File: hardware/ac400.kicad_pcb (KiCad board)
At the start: 2 copper layers, 105.4 x 76.2 mm, 71 parts, among them J1 AVR-ISP-10, J2 LOW OUT, J3 MID OUT, J4 HIGH OUT, J5 COMMON OUT, J6 COMMON IN, J7 LINE IN, J8 3.3V IN, K1 SRD-03VDC-SL-C, K2 SRD-03VDC-SL-C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

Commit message: "final" touches on v1 board
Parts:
- added SYM2: Julian7 logo, ac400:Julian7 maker's mark, F.Cu at (148.1, 117.3)
- C2: footprint PCM_Capacitor_THT_AKL:C_Radial_D8.0mm_H11.5mm_P3.50mm -> Capacitor_THT:CP_Radial_D8.0mm_P3.50mm
- D1, D2, D3: footprint Diode_SMD:D_0805_2012Metric_Pad1.15x1.40mm_HandSolder -> Diode_SMD:D_SOD-323
- TP5: value MG -> MD
- TP6: value MD -> MG
- TP7: value HG -> HD
- TP8: value HD -> HG
- moved R16 8.70 mm to (171.2, 116.5), turned to 90 degrees
- moved C13 5.39 mm to (85.1, 120.5), turned to 90 degrees
- moved R17 5.16 mm to (86.9, 126.1), turned to 90 degrees
- moved C2 3.98 mm to (115.3, 97.9), turned to 90 degrees
- moved TP8 3.56 mm to (137.2, 89.0)
- moved JP1 3.16 mm to (173.7, 108.6), turned to 90 degrees
- moved TP6 3.11 mm to (154.7, 89.0), turned to 180 degrees
- moved TP5 2.96 mm to (154.7, 92.0), turned to 180 degrees
- moved R1 2.74 mm to (170.3, 96.2)
- moved Q4 2.45 mm to (90.4, 126.1), turned to -90 degrees
- moved TP7 2.44 mm to (137.2, 92.0)
- moved C8 1.88 mm to (131.1, 94.2), turned to 90 degrees
- moved C6 1.86 mm to (165.6, 94.2), turned to 90 degrees
- moved C9 1.85 mm to (163.2, 94.2), turned to 90 degrees
- moved TP3 1.82 mm to (173.0, 92.0)
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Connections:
- net Net-(BZ1--) renamed /Buzz Drain
- net Net-(D1-A) renamed /Low Drain
- net Net-(J2-Pin_1) renamed /LOW OUT
- net Net-(J3-Pin_1) renamed /MID OUT
- net Net-(J4-Pin_1) renamed /HIGH OUT
- D2 pad 2: Net-(D2-A) -> /Mid Drain
- D3 pad 2: Net-(D3-A) -> /High Drain
- K2 pad 2: Net-(D2-A) -> /Mid Drain
- K3 pad 2: Net-(D3-A) -> /High Drain
- Q2 pad 3: Net-(D2-A) -> /Mid Drain
- Q3 pad 3: Net-(D3-A) -> /High Drain
- TP5 pad 1: Net-(Q2-G) -> /Mid Drain
- TP6 pad 1: Net-(D2-A) -> Net-(Q2-G)
- TP7 pad 1: Net-(Q3-G) -> /High Drain
- TP8 pad 1: Net-(D3-A) -> Net-(Q3-G)
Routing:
- net +3.3V: track 274.7 -> 250.3 mm
- net Net-(D2-A): track 21.8 -> 0.00 mm, vias 2 -> 0
- net Net-(D3-A): track 21.6 -> 0.00 mm, vias 2 -> 0
- net /Mid Drain: track 0.00 -> 21.0 mm, vias 0 -> 2
- net /High Drain: track 0.00 -> 20.8 mm, vias 0 -> 2
- net Net-(Q3-G): track 19.8 -> 10.7 mm
- net BUZZ: track 71.4 -> 77.5 mm
- net HIGH: track 35.2 -> 40.8 mm
- net Net-(Q2-G): track 14.8 -> 10.2 mm
- net Net-(Q4-G): track 8.82 -> 4.87 mm
- net NEUT: track 39.8 -> 43.7 mm
- net MISO: track 20.3 -> 16.9 mm
- net LOW: track 15.9 -> 13.2 mm
- net Net-(Q1-G): track 12.7 -> 10.7 mm
- net GND: track 26.8 -> 25.2 mm, vias 101 -> 107
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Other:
- board text added: "AC-400 controller"
- board text added: "COMMON IN"
- board text added: "COMMON OUT"
- board text added: "HIGH OUT"
- board text added: "LINE IN"
- board text added: "LOW OUT"
- board text added: "MID OUT"

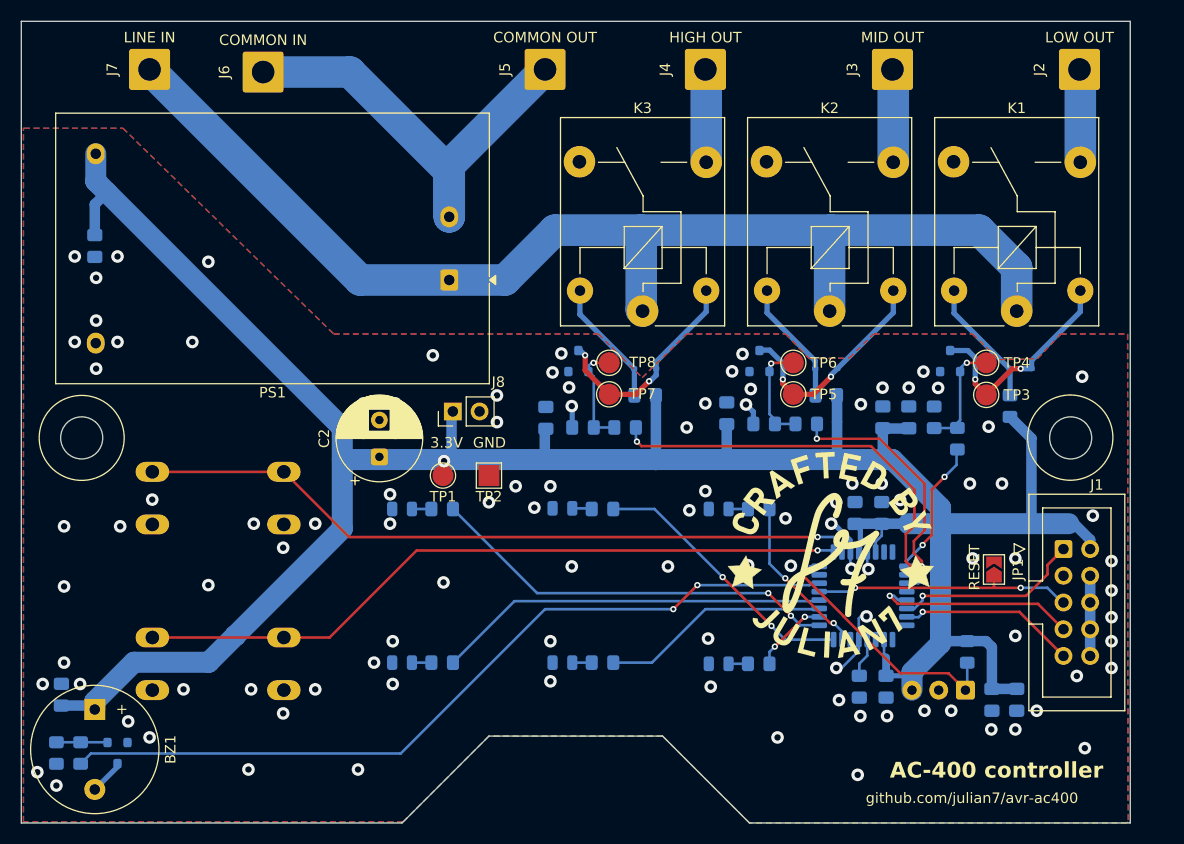
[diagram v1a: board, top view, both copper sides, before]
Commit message: mounting holes distance and library references fix
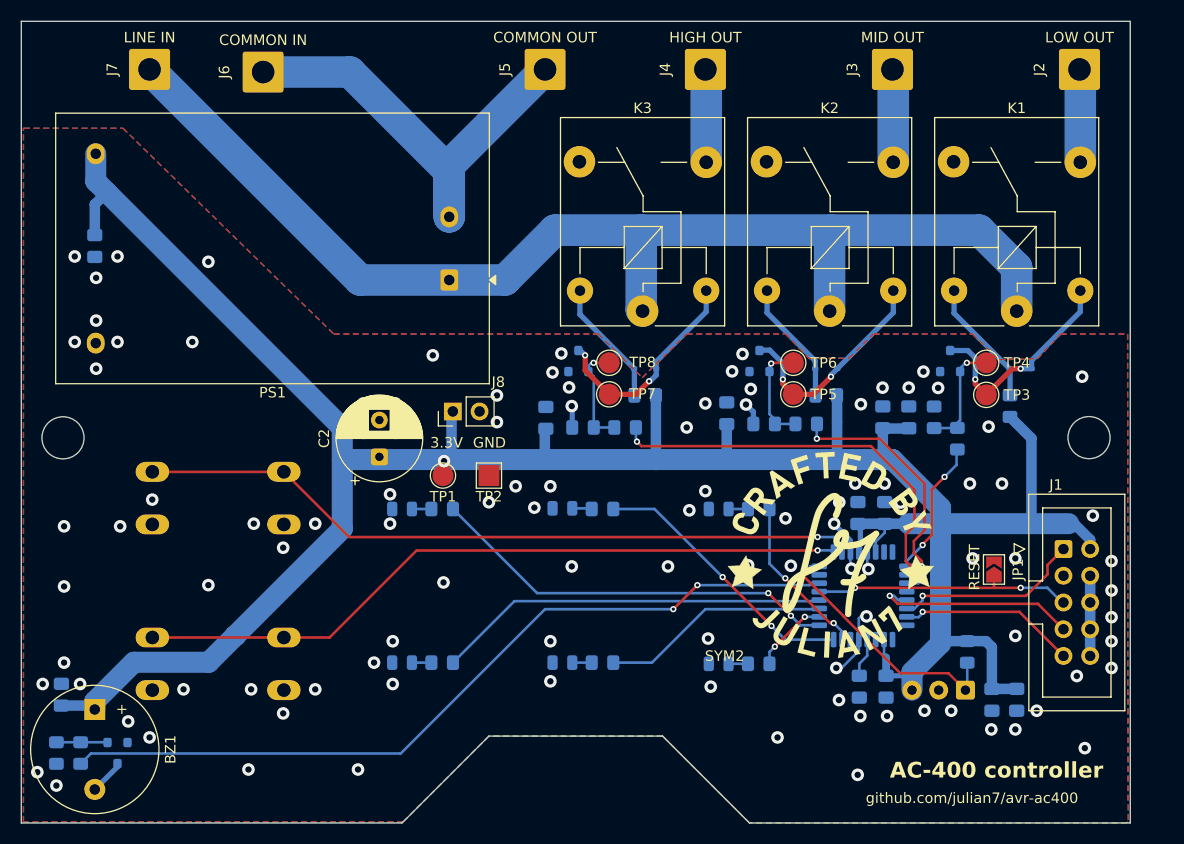
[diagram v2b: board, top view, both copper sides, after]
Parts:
- SYM1: footprint ac400:AC400 Board -> ac400:board_shape
- SYM2: footprint ac400:Julian7 maker's mark -> ac400:julian7_makers_mark
- moved C12 0.28 mm to (160.8, 103.3)
- moved C1 0.28 mm to (163.3, 103.3)
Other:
- outline, holes or cut-outs redrawn
